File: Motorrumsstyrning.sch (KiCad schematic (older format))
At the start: 10 parts

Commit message: Added symbols, worked on schematic and PCB
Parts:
- removed U?: uA7805, symbol Regulator_Linear:uA7805
- added IC1: MCP2562-E_P, Vera-MRS-21:DIP781W56P254L950H533Q8N, symbol Vera-MRS-21:MCP2562-E_P
- added J1: SD_Card_Connector, Vera-MRS-21:2041021-3_2, symbol Vera-MRS-21:SD_Card_Connector
- added R1, R2, R3, R4, R5, R6, R7: 50k, Resistor_THT:R_Axial_DIN0204_L3.6mm_D1.6mm_P5.08mm_Horizontal, symbol Device:R_Small
- added R12: 120R, Resistor_THT:R_Axial_DIN0204_L3.6mm_D1.6mm_P5.08mm_Horizontal, symbol Device:R_Small
- added R8: 4k2, Resistor_THT:R_Axial_DIN0204_L3.6mm_D1.6mm_P5.08mm_Horizontal, symbol Device:R_Small
- added R9: 10k, Resistor_THT:R_Axial_DIN0204_L3.6mm_D1.6mm_P5.08mm_Horizontal, symbol Device:R_Small
- added U1: LM1084-5.0, Package_TO_SOT_THT:TO-220-3_Vertical, symbol Regulator_Linear:LM1084-5.0
- added U2: NUCLEO-F303K8, Vera-MRS-21:NUCLEO_32, symbol Vera-MRS-21:NUCLEO-F303K8
- J2: renamed from J?; footprint (none) -> TerminalBlock_Phoenix:TerminalBlock_Phoenix_MPT-0,5-10-2.54_1x10_P2.54mm_Horizontal
- R10, R11: renamed from R?; footprint (none) -> Resistor_THT:R_Axial_DIN0204_L3.6mm_D1.6mm_P5.08mm_Horizontal
- gave numbers to parts that had none: 2
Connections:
- net labels added: +3V3, CANH, CANL, CAN_RX, CAN_TX, Deadmans, I2C1_SCL, I2C1_SDA, SPI1_MISO, SPI1_MOSI, SPI1_SCK, Tach_12V, Tachometer, USAR2_RX, USART2_TX, ~CD, ~SPI1_CS, ~WP
- net labels removed: Deadmans_3V3
- wire segments 22 -> 67
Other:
- note added: "-1. Se om uA7805 eller annan 12-5V finns, annars byt regulator"
- note added: "5. Verifiera att VREF är kopplad till VDD på NUCLEO genom lödbrygga enligt datablad."
- note added: "6. Filtrera och begränsa +12V om VIN är kopplad till den."
- note added: "CAN Transceiver"
- note added: "Mounting Hole Grounding"
- note added: "Onödig iom LDO på NUCLEO?"
- note added: "SD-Card Holder"
- note added: "SD-kort drivers: https://github.com/kiwih/cubemx-mmc-sd-card"
- note added: "Screw Terminal"
- note removed: "1. Se om uA7805 eller annan 12-5V finns, annars byt regulator"
- moved on the sheet: C1, C2, H1, H2, H3, H4, J2, R10, R11

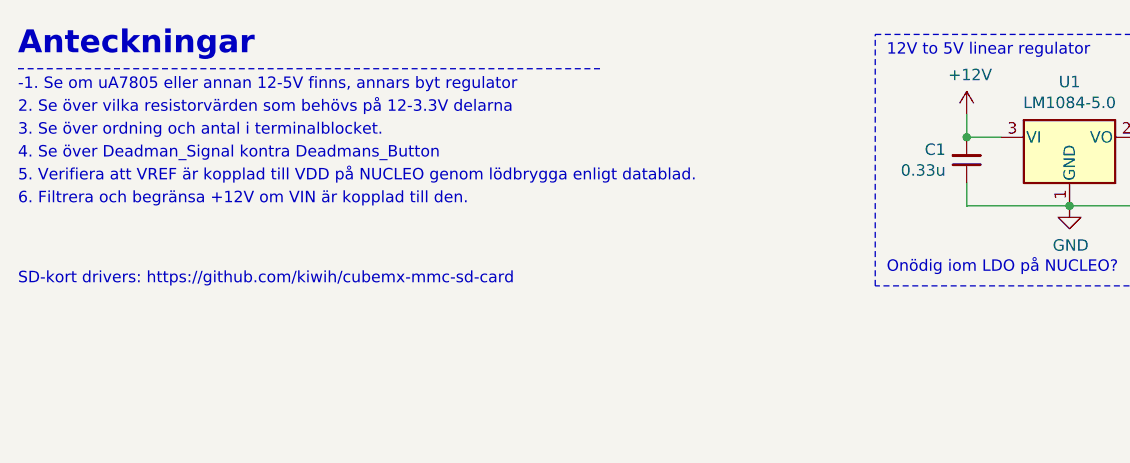
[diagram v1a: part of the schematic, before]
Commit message: Large PCB first design
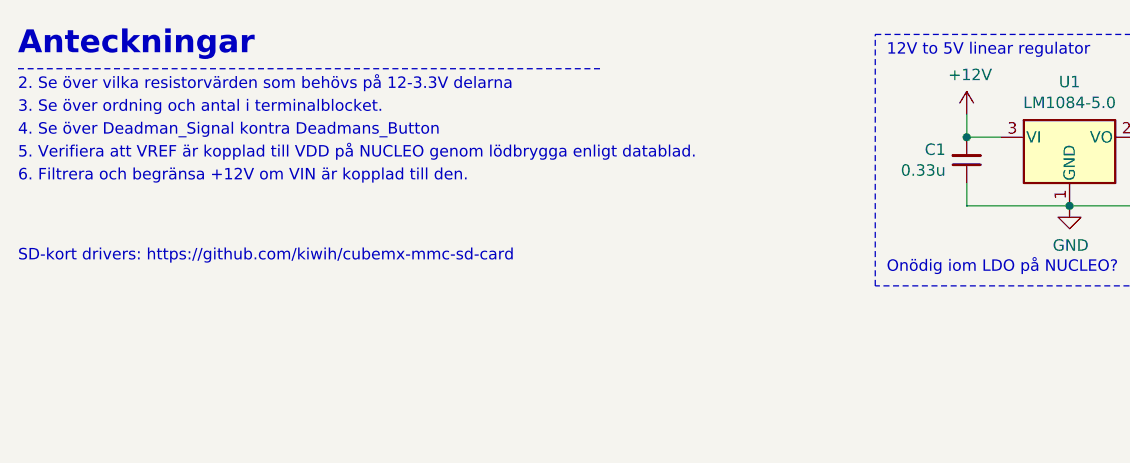
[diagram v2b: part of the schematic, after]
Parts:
- U1: footprint Package_TO_SOT_THT:TO-220-3_Vertical -> Package_TO_SOT_THT:TO-220-3_Horizontal_TabDown
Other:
- note removed: "-1. Se om uA7805 eller annan 12-5V finns, annars byt regulator"
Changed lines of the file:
@@
 Wire Wire Line
 	10600 4550 10600 4450
+Text Notes 500  800  0    50   ~ 0
+2. Se över vilka resistorvärden som behövs på 12-3.3V delarna
 Text Notes 500  900  0    50   ~ 0
-2. Se över vilka resistorvärden som behövs på 12-3.3V delarna
-Text Notes 500  1000 0    50   ~ 0
 3. Se över ordning och antal i terminalblocket.
 Text Label 10700 5750 2    50   ~ 0
@@
 Wire Wire Line
 	10700 5750 10100 5750
-Text Notes 500  1100 0    50   ~ 0
+Text Notes 500  1000 0    50   ~ 0
 4. Se över Deadman_Signal kontra Deadmans_Button
 Wire Notes Line
@@
 Wire Wire Line
 	800  7400 800  7500
-Text Notes 500  1200 0    50   ~ 0
+Text Notes 500  1100 0    50   ~ 0
 5. Verifiera att VREF är kopplad till VDD på NUCLEO genom lödbrygga enligt datablad.
 $Comp
@@
 	1    0    0    -1
 $EndComp
-Text Notes 500  1650 0    50   ~ 0
+Text Notes 500  1550 0    50   ~ 0
 SD-kort drivers: https://github.com/kiwih/cubemx-mmc-sd-card
 $Comp
@@
 	1    0    0    -1
 $EndComp
-Text Notes 500  800  0    50   ~ 0
--1. Se om uA7805 eller annan 12-5V finns, annars byt regulator
-Text Notes 500  1300 0    50   ~ 0
+Text Notes 500  1200 0    50   ~ 0
 6. Filtrera och begränsa +12V om VIN är kopplad till den.
 $Comp
@@
 F 0 "U1" H 5100 1242 50  0000 C CNN
 F 1 "LM1084-5.0" H 5100 1151 50  0000 C CNN
-F 2 "Package_TO_SOT_THT:TO-220-3_Vertical" H 5100 1250 50  0001 C CIN
+F 2 "Package_TO_SOT_THT:TO-220-3_Horizontal_TabDown" H 5100 1250 50  0001 C CIN
 F 3 "http://www.ti.com/lit/ds/symlink/lm1084.pdf" H 5100 1000 50  0001 C CNN
 	1    5100 1000
